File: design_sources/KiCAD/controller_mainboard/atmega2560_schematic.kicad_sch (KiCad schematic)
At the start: 18 parts, among them J16 02x03_pinheader, SW1 SW_Push, U1 ATmega2560-16A, Y1 16MHz

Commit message: Advanced the hardware layout further.
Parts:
- added C92: 50V 22pF C0G, Capacitor_SMD:C_0402_1005Metric, symbol Device:C
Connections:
- net GND: now also C92.1
- net ~{RESET}: now also C92.2
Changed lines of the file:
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@@
 	(wire
 		(pts
+			(xy 248.92 43.18) (xy 248.92 46.99)
+		)
+		(stroke
+			(width 0)
+			(type default)
+		)
+	)
+	(wire
+		(pts
 			(xy 127 96.52) (xy 127 93.98)
 		)
@@
 	(wire
 		(pts
+			(xy 248.92 57.15) (xy 248.92 59.69)
+		)
+		(stroke
+			(width 0)
+			(type default)
+		)
+	)
+	(wire
+		(pts
 			(xy 151.13 158.75) (xy 154.94 158.75)
 		)
@@
 	(wire
 		(pts
-			(xy 200.66 118.11) (xy 195.58 118.11)
+			(xy 248.92 46.99) (xy 248.92 49.53)
 		)
 		(stroke
@@
 	(wire
 		(pts
-			(xy 200.66 92.71) (xy 195.58 92.71)
+			(xy 200.66 118.11) (xy 195.58 118.11)
 		)
 		(stroke
@@
 	(wire
 		(pts
-			(xy 119.38 40.64) (xy 119.38 54.61)
+			(xy 200.66 92.71) (xy 195.58 92.71)
 		)
 		(stroke
@@
 	(wire
 		(pts
-			(xy 231.14 116.84) (xy 231.14 118.11)
+			(xy 119.38 40.64) (xy 119.38 54.61)
 		)
 		(stroke
@@
 	(wire
 		(pts
-			(xy 175.26 204.47) (xy 175.26 208.28)
+			(xy 231.14 116.84) (xy 231.14 118.11)
 		)
 		(stroke
@@
 	(wire
 		(pts
-			(xy 151.13 87.63) (xy 154.94 87.63)
+			(xy 175.26 204.47) (xy 175.26 208.28)
 		)
 		(stroke
@@
 	(wire
 		(pts
-			(xy 248.92 43.18) (xy 248.92 46.99)
+			(xy 151.13 87.63) (xy 154.94 87.63)
 		)
 		(stroke
@@
 	(symbol
 		(lib_id "power:GND")
+		(at 248.92 59.69 0)
+		(unit 1)
+		(exclude_from_sim no)
+		(in_bom yes)
+		(on_board yes)
+		(dnp no)
+		(fields_autoplaced yes)
+		(property "Reference" "#PWR0132"
+			(at 248.92 66.04 0)
+			(effects
+				(font
+					(size 1.27 1.27)
+				)
+				(hide yes)
+			)
+		)
+		(property "Value" "GND"
+			(at 248.92 64.77 0)
+			(effects
+				(font
+					(size 1.27 1.27)
+				)
+				(hide yes)
+			)
+		)
+		(property "Footprint" ""
+			(at 248.92 59.69 0)
+			(effects
+				(font
+					(size 1.27 1.27)
+				)
+				(hide yes)
+			)
+		)
+		(property "Datasheet" ""
+			(at 248.92 59.69 0)
+			(effects
+				(font
+					(size 1.27 1.27)
+				)
+				(hide yes)
+			)
+		)
+		(property "Description" "Power symbol creates a global label with name \"GND\" , ground"
+			(at 248.92 59.69 0)
+			(effects
+				(font
+					(size 1.27 1.27)
+				)
+				(hide yes)
+			)
+		)
+		(pin "1"
+		)
+		(instances
+			(project "controller_mainboard"
+				(path "/0fdfffec-3d24-4249-8ba9-dae7a6ccc250/104cadd7-dded-4cf0-b82f-f956a8bd9cde"
+					(reference "#PWR0132")
+					(unit 1)
+				)
+			)
+		)
+	)
+	(symbol
+		(lib_id "power:GND")
 		(at 153.67 55.88 0)
 		(unit 1)
@@
 					(unit 1)
 				)
+			)
+		)
+	)
+	(symbol
+		(lib_id "Device:C")
+		(at 248.92 53.34 180)
+		(unit 1)
+		(exclude_from_sim no)
+		(in_bom yes)
+		(on_board yes)
+		(dnp no)
+		(fields_autoplaced yes)
+		(property "Reference" "C92"
+			(at 252.73 52.0699 0)
+			(effects
+				(font
+					(size 1.27 1.27)
+				)
+				(justify right)
+			)
+		)
+		(property "Value" "50V 22pF C0G"
+			(at 252.73 54.6099 0)
+			(effects
+				(font
+					(size 1.27 1.27)
+				)
+				(justify right)
+			)
+		)
+		(property "Footprint" "Capacitor_SMD:C_0402_1005Metric"
+			(at 247.9548 49.53 0)
+			(effects
+				(font
+					(size 1.27 1.27)
+				)
+				(hide yes)
+			)
+		)
+		(property "Datasheet" "https://jlcpcb.com/api/file/downloadByFileSystemAccessId/8579707297419231232"
+			(at 248.92 53.34 0)
+			(effects
+				(font
+					(size 1.27 1.27)
+				)
+				(hide yes)
+			)
+		)
+		(property "Description" "Unpolarized capacitor"
+			(at 248.92 53.34 0)
+			(effects
+				(font
+					(size 1.27 1.27)
+				)
+				(hide yes)
+			)
+		)
+		(property "JLCPCB" "C1555"
+			(at 248.92 53.34 90)
+			(effects
+				(font
+					(size 1.27 1.27)
+				)
+				(hide yes)
+			)
+		)
+		(pin "2"
+		)
+		(pin "1"
+		)
+		(instances
+			(project "controller_mainboard"
+				(path "/0fdfffec-3d24-4249-8ba9-dae7a6ccc250/104cadd7-dded-4cf0-b82f-f956a8bd9cde"
+					(reference "C92")
+					(unit 1)
+				)

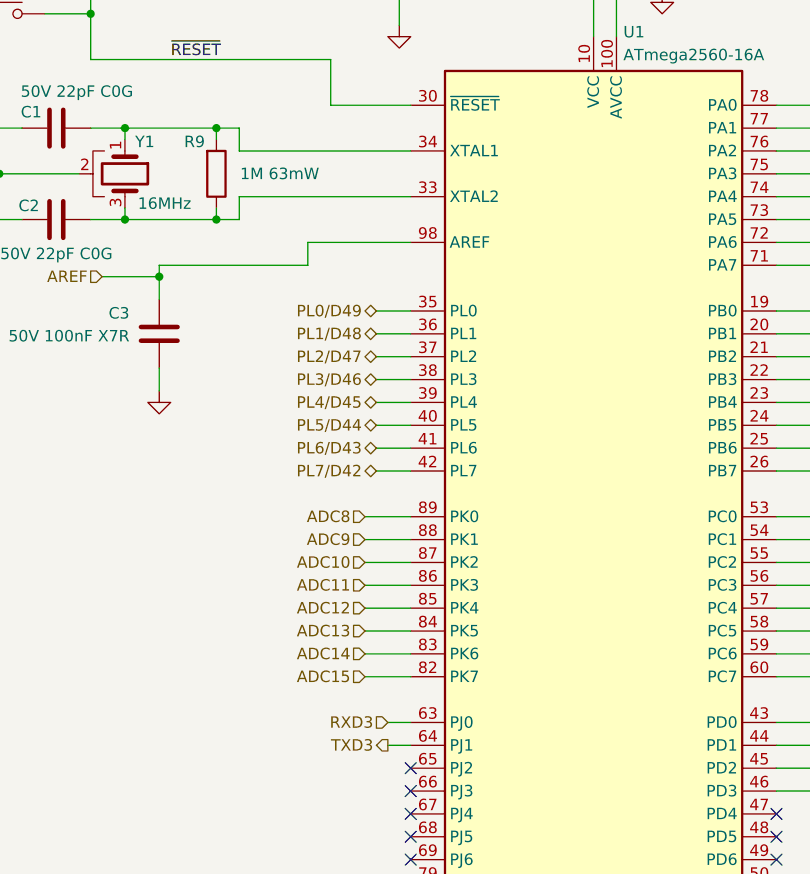
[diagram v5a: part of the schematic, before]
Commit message: Re-checked DRC, differing footprint warnings are fine, added production files for JLC placement and prod. TODO, maybe cool silk art at the bottom and definitive order list.
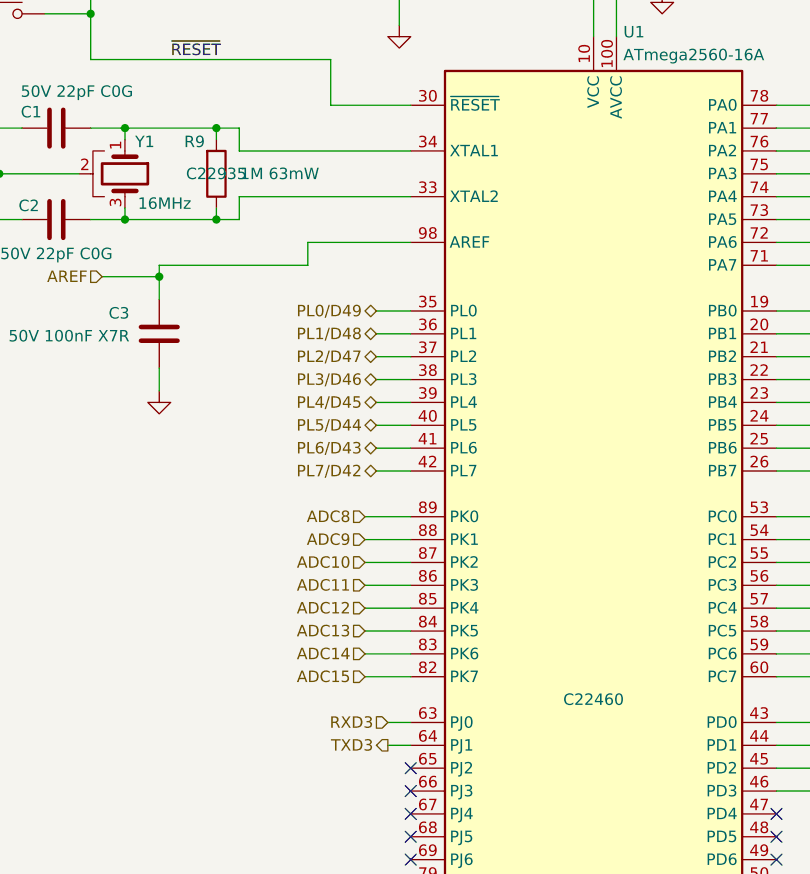
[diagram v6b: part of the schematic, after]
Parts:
- R9: JLCPCB (none) -> C22935
- U1: JLCPCB (none) -> C22460
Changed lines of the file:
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@@
+			)
+		)
+		(property "JLCPCB" "C22935"
+			(at 133.35 72.39 0)
+			(effects
+				(font
+					(size 1.27 1.27)
+				)
 			)
 		)
@@
 			)
 		)
+		(property "JLCPCB" "C22460"
+			(at 175.26 130.81 0)
+			(effects
+				(font
+					(size 1.27 1.27)
+				)
+			)
+		)

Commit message: Changed JLCPCB field to LCSC
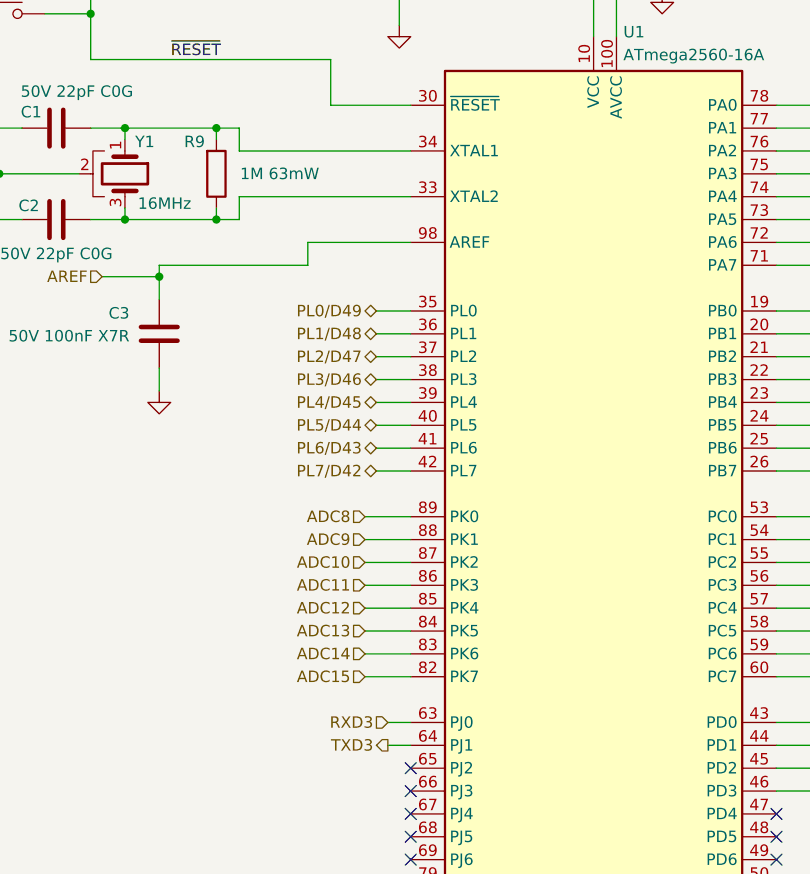
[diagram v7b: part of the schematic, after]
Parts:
- C1, C2, C92: JLCPCB C1555 -> (none); LCSC (none) -> C1555
- C3, C5, C6, C8: JLCPCB C14663 -> (none); LCSC (none) -> C14663
- C4: JLCPCB C5246561 -> (none); LCSC (none) -> C5246561
- C7: JLCPCB C15849 -> (none); LCSC (none) -> C15849
- D3: JLCPCB C22452 -> (none); LCSC (none) -> C22452
- L1: JLCPCB C1046 -> (none); LCSC (none) -> C1046
- R10, R90, R91: JLCPCB C25744 -> (none); LCSC (none) -> C25744
- R9: JLCPCB C22935 -> (none); LCSC (none) -> C22935
- SW1: JLCPCB C19191552 -> (none); LCSC (none) -> C19191552
- U1: JLCPCB C22460 -> (none); LCSC (none) -> C22460
- Y1: JLCPCB C783275 -> (none); LCSC (none) -> C783275
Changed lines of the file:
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@@
 			)
 		)
-		(property "JLCPCB" "C14663"
+		(property "LCSC" "C14663"
 			(at 182.88 46.99 0)
 			(effects
@@
 			)
 		)
-		(property "JLCPCB" "C15849"
+		(property "LCSC" "C15849"
 			(at 166.37 41.91 0)
 			(effects
@@
 			)
 		)
-		(property "JLCPCB" "C25744"
+		(property "LCSC" "C25744"
 			(at 248.92 39.37 0)
 			(effects
@@
 			)
 		)
-		(property "JLCPCB" "C14663"
+		(property "LCSC" "C14663"
 			(at 157.48 41.91 0)
 			(effects
@@
 			)
 		)
-		(property "JLCPCB" "C25744"
+		(property "LCSC" "C25744"
 			(at 238.76 121.92 0)
 			(effects
@@
 			)
 		)
-		(property "JLCPCB" "C19191552"
+		(property "LCSC" "C19191552"
 			(at 109.22 54.61 0)
 			(effects
@@
 			)
 		)
-		(property "JLCPCB" "C22935"
+		(property "LCSC" "C22935"
 			(at 133.35 72.39 0)
 			(effects
@@
 					(size 1.27 1.27)
 				)
+				(hide yes)
 			)
 		)
@@
 			)
 		)
-		(property "JLCPCB" "C1555"
+		(property "LCSC" "C1555"
 			(at 115.57 77.47 90)
 			(effects
@@
 			)
 		)
-		(property "JLCPCB" "C14663"
+		(property "LCSC" "C14663"
 			(at 148.59 41.91 0)
 			(effects
@@
 			)
 		)
-		(property "JLCPCB" "C14663"
+		(property "LCSC" "C14663"
 			(at 127 90.17 0)
 			(effects
@@
 			)
 		)
-		(property "JLCPCB" "C22452"
+		(property "LCSC" "C22452"
 			(at 232.41 39.37 90)
 			(effects
@@
 			)
 		)
-		(property "JLCPCB" "C783275"
+		(property "LCSC" "C783275"
 			(at 123.19 72.39 90)
 			(effects
@@
 			)
 		)
-		(property "JLCPCB" "C22460"
+		(property "LCSC" "C22460"
 			(at 175.26 130.81 0)
 			(effects
@@
 					(size 1.27 1.27)
 				)
+				(hide yes)
 			)
 		)
@@
 			)
 		)
-		(property "JLCPCB" "C1555"
+		(property "LCSC" "C1555"
 			(at 115.57 67.31 90)
 			(effects
@@
 			)
 		)
-		(property "JLCPCB" "C25744"
+		(property "LCSC" "C25744"
 			(at 231.14 121.92 0)
 			(effects
@@
 			)
 		)
-		(property "JLCPCB" "C5246561"
+		(property "LCSC" "C5246561"
 			(at 139.7 41.91 0)
 			(effects
@@
 			)
 		)
-		(property "JLCPCB" "C1555"
-			(at 248.92 53.34 90)
+		(property "LCSC" "C1555"
+			(at 248.92 53.34 0)
 			(effects
 				(font
@@
 			)
 		)
-		(property "JLCPCB" "C1046"
+		(property "LCSC" "C1046"
 			(at 177.8 36.83 0)
 			(effects
